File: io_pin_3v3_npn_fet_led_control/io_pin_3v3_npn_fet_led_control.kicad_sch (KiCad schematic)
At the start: 8 parts, among them Q3 NMOS

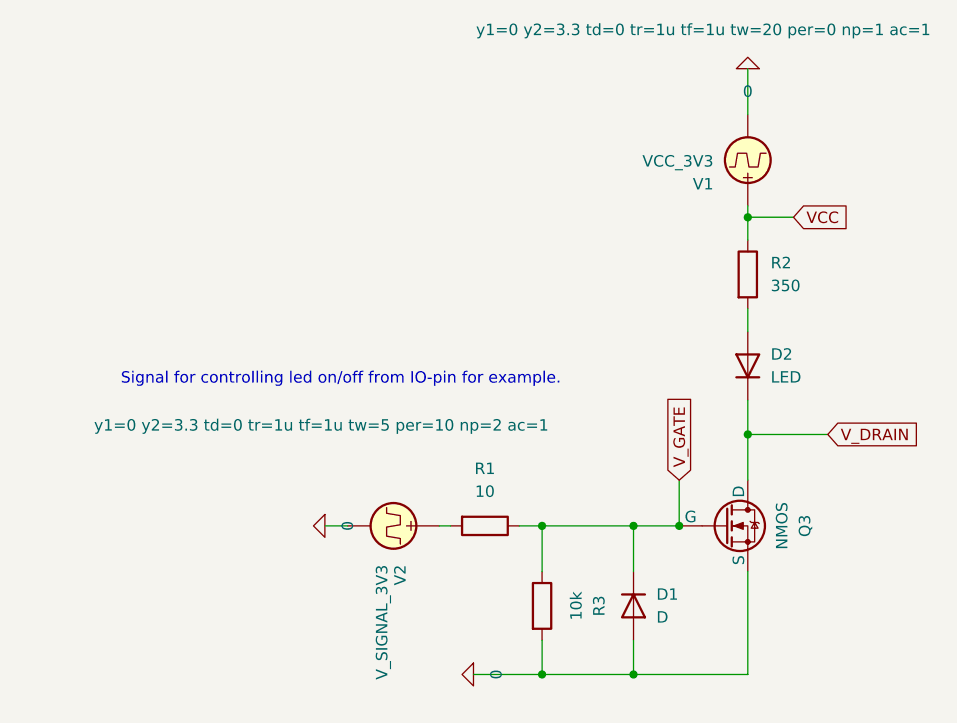
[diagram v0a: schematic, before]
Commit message: drop led voltage in 3v3 npn fet example
Signed-off-by: Mika Laitio <lamikr@gmail.com>
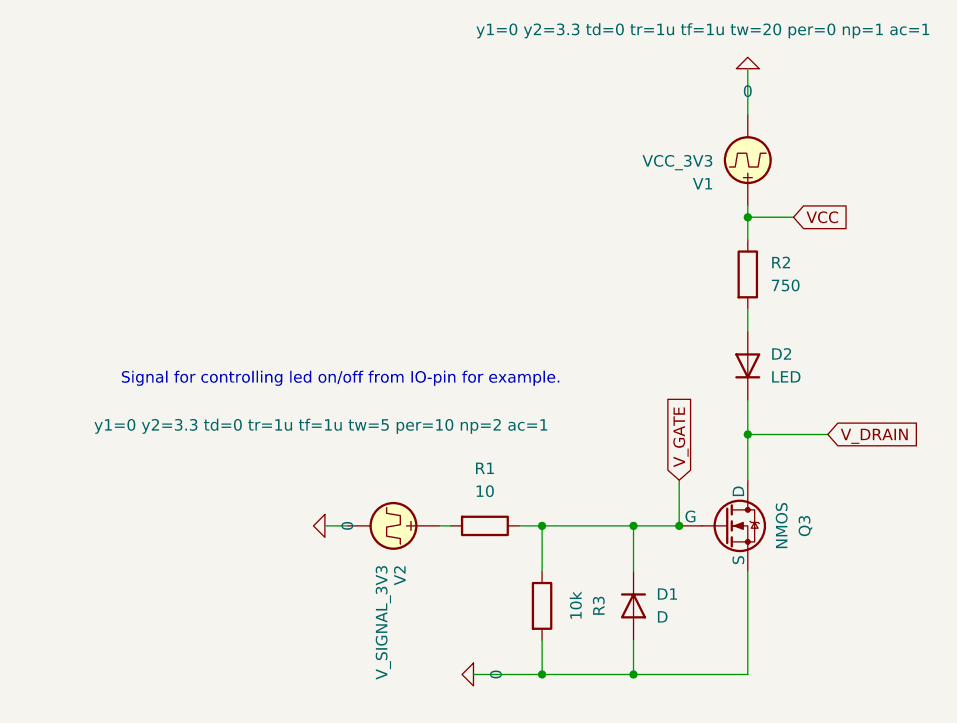
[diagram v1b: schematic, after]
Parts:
- R2: value 350 -> 750
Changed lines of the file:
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@@
 			)
 		)
-		(property "Value" "350"
+		(property "Value" "750"
 			(at 95.25 48.2599 0)
 			(effects
